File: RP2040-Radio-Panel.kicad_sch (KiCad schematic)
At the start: 1 part, among them U1 DM13A

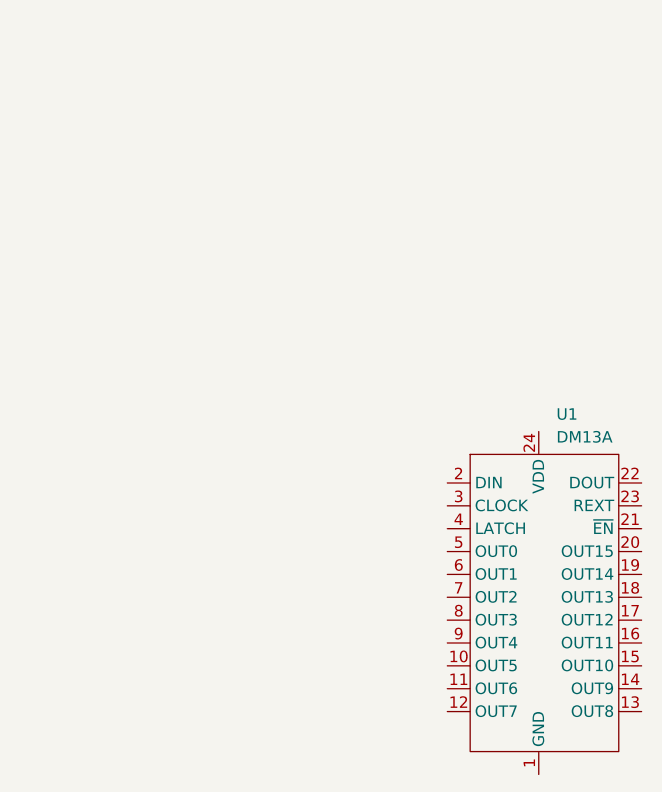
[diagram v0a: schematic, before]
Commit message: Add RP2040
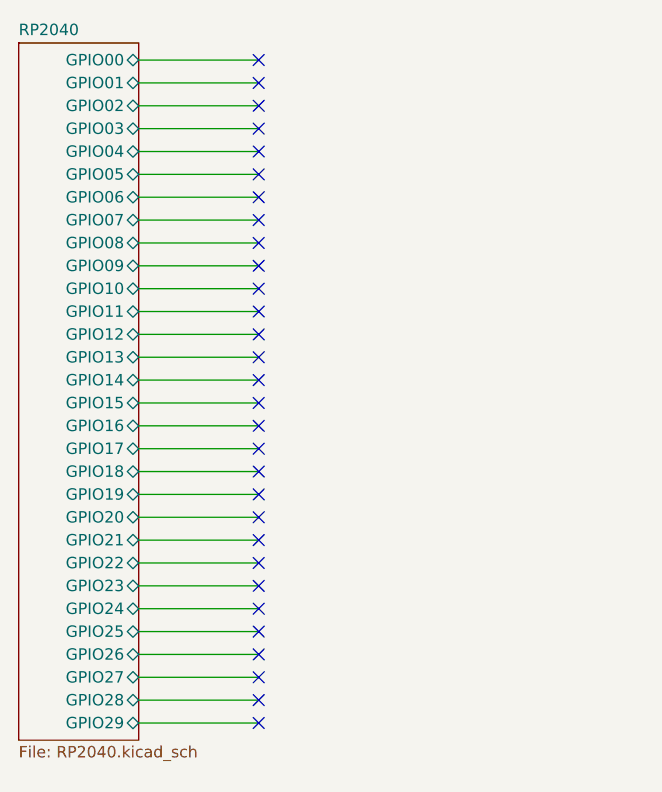
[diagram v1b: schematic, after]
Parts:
- removed U1: DM13A, Package_SO:SSOP-24_3.9x8.7mm_P0.635mm, symbol Custom_Symbols:DM13A
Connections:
- no-connect marks 0 -> 30
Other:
- added sheet RP2040 (RP2040.kicad_sch)

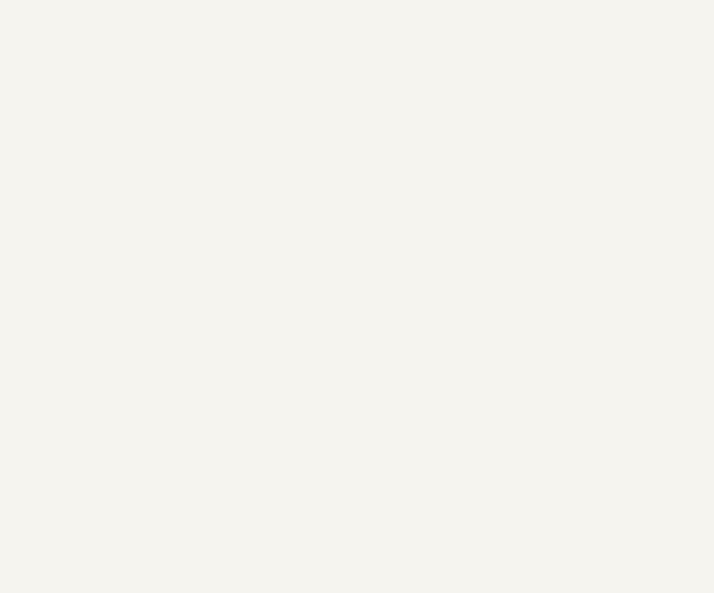
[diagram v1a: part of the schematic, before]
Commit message: Add a level shifter
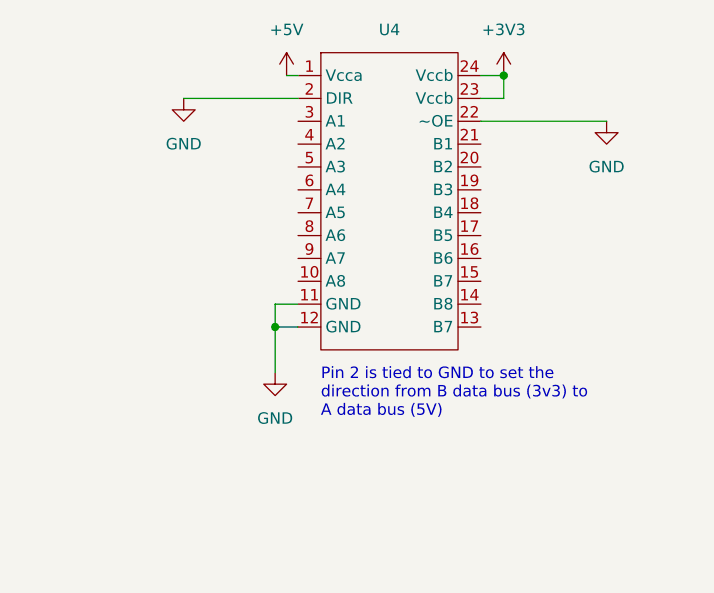
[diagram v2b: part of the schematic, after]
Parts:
- added U4: ~, Package_SO:TSSOP-24_4.4x7.8mm_P0.65mm, symbol Custom_Symbols:SN74LVC4245APWR
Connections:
- new net +3V3: U4.23 (Vccb), U4.24 (Vccb)
- new net +5V: U4.1 (Vcca)
- new net GND: U4.11 (GND), U4.12 (GND), U4.2 (DIR), U4.22 (~OE)
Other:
- note added: "Pin 2 is tied to GND to set the direction from B data bus (3v3) to A data bus (5V)"
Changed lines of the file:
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@@
     (rev "${VERSION}")
+  )
+  (junction (at 113.03 20.32) (diameter 0) (color 0 0 0 0)
+  )
+  (junction (at 87.63 48.26) (diameter 0) (color 0 0 0 0)
   )
   (no_connect (at 41.275 74.93))
@@
     (stroke (width 0) (type default))
   )
+  (wire (pts (xy 110.49 20.32) (xy 113.03 20.32))
+    (stroke (width 0) (type default))
+  )
+  (wire (pts (xy 87.63 48.26) (xy 87.63 53.34))
+    (stroke (width 0) (type default))
+  )
   (wire (pts (xy 27.94 72.39) (xy 41.275 72.39))
     (stroke (width 0) (type default))
   )
+  (wire (pts (xy 77.47 22.86) (xy 90.17 22.86))
+    (stroke (width 0) (type default))
+  )
+  (wire (pts (xy 110.49 22.86) (xy 113.03 22.86))
+    (stroke (width 0) (type default))
+  )
   (wire (pts (xy 27.94 92.71) (xy 41.275 92.71))
     (stroke (width 0) (type default))
@@
     (stroke (width 0) (type default))
   )
+  (wire (pts (xy 88.9 20.32) (xy 90.17 20.32))
+    (stroke (width 0) (type default))
+  )
+  (wire (pts (xy 110.49 25.4) (xy 124.46 25.4))
+    (stroke (width 0) (type default))
+  )
+  (wire (pts (xy 90.17 45.72) (xy 87.63 45.72))
+    (stroke (width 0) (type default))
+  )
   (wire (pts (xy 27.94 69.85) (xy 41.275 69.85))
     (stroke (width 0) (type default))
@@
     (stroke (width 0) (type default))
   )
+  (wire (pts (xy 87.63 48.26) (xy 90.17 48.26))
+    (stroke (width 0) (type default))
+  )
   (wire (pts (xy 27.94 31.75) (xy 41.275 31.75))
     (stroke (width 0) (type default))
   )
+  (wire (pts (xy 87.63 45.72) (xy 87.63 48.26))
+    (stroke (width 0) (type default))
+  )
+  (wire (pts (xy 113.03 22.86) (xy 113.03 20.32))
+    (stroke (width 0) (type default))
+  )
   (wire (pts (xy 27.94 62.23) (xy 41.275 62.23))
     (stroke (width 0) (type default))
@@
     (stroke (width 0) (type default))
   )
+  (text "Pin 2 is tied to GND to set the\ndirection from B data bus (3v3) to\nA data bus (5V)"
+    (at 92.71 58.42 0)
+    (effects (font (size 1.27 1.27)) (justify left bottom))
+  )
+  (symbol (lib_id "power:GND") (at 77.47 22.86 0) (unit 1)
+    (in_bom yes) (on_board yes) (dnp no) (fields_autoplaced)
+    (property "Reference" "#PWR08" (at 77.47 29.21 0)
+      (effects (font (size 1.27 1.27)) hide)
+    )
+    (property "Value" "GND" (at 77.47 27.94 0)
+      (effects (font (size 1.27 1.27)))
+    )
+    (property "Footprint" "" (at 77.47 22.86 0)
+      (effects (font (size 1.27 1.27)) hide)
+    )
+    (property "Datasheet" "" (at 77.47 22.86 0)
+      (effects (font (size 1.27 1.27)) hide)
+    )
+    (pin "1")
+    (instances
+      (project "RP2040-Radio-Panel"
+        (path "/e63e39d7-6ac0-4ffd-8aa3-1841a4541b55"
+          (reference "#PWR08") (unit 1)
+        )
+      )
+    )
+  )
+  (symbol (lib_id "power:+5V") (at 88.9 20.32 0) (unit 1)
+    (in_bom yes) (on_board yes) (dnp no) (fields_autoplaced)
+    (property "Reference" "#PWR03" (at 88.9 24.13 0)
+      (effects (font (size 1.27 1.27)) hide)
+    )
+    (property "Value" "+5V" (at 88.9 15.24 0)
+      (effects (font (size 1.27 1.27)))
+    )
+    (property "Footprint" "" (at 88.9 20.32 0)
+      (effects (font (size 1.27 1.27)) hide)
+    )
+    (property "Datasheet" "" (at 88.9 20.32 0)
+      (effects (font (size 1.27 1.27)) hide)
+    )
+    (pin "1")
+    (instances
+      (project "RP2040-Radio-Panel"
+        (path "/e63e39d7-6ac0-4ffd-8aa3-1841a4541b55"
+          (reference "#PWR03") (unit 1)
+        )
+      )
+    )
+  )
+  (symbol (lib_id "Custom_Symbols:SN74LVC4245APWR") (at 100.33 34.29 0) (unit 1)
+    (in_bom yes) (on_board yes) (dnp no) (fields_autoplaced)
+    (property "Reference" "U4" (at 100.33 15.24 0)
+      (effects (font (size 1.27 1.27)))
+    )
+    (property "Value" "~" (at 90.17 20.32 0)
+      (effects (font (size 1.27 1.27)))
+    )
+    (property "Footprint" "Package_SO:TSSOP-24_4.4x7.8mm_P0.65mm" (at 100.33 55.88 0)
+      (effects (font (size 1.27 1.27)) hide)
+    )
+    (property "Datasheet" "https://www.ti.com/general/docs/suppproductinfo.tsp?distId=10&gotoUrl=https%3A%2F%2Fwww.ti.com%2Flit%2Fgpn%2Fsn74lvc4245a" (at 100.33 53.34 0)
+      (effects (font (size 1.27 1.27)) hide)
+    )
+    (property "MPN - JLCPCB" "C7859" (at 100.33 34.29 0)
+      (effects (font (size 1.27 1.27)) hide)
+    )
+    (pin "1")
+    (pin "10")
+    (pin "11")
+    (pin "12")
+    (pin "13")
+    (pin "14")
+    (pin "15")
+    (pin "16")
+    (pin "17")
+    (pin "18")
+    (pin "19")
+    (pin "2")
+    (pin "20")
+    (pin "21")
+    (pin "22")
+    (pin "23")
+    (pin "24")
+    (pin "3")
+    (pin "4")
+    (pin "5")
+    (pin "6")
+    (pin "7")
+    (pin "8")
+    (pin "9")
+    (instances
+      (project "RP2040-Radio-Panel"
+        (path "/e63e39d7-6ac0-4ffd-8aa3-1841a4541b55"
+          (reference "U4") (unit 1)
+        )
+      )
+    )
+  )
+  (symbol (lib_id "power:+3V3") (at 113.03 20.32 0) (unit 1)
+    (in_bom yes) (on_board yes) (dnp no) (fields_autoplaced)
+    (property "Reference" "#PWR04" (at 113.03 24.13 0)
+      (effects (font (size 1.27 1.27)) hide)
+    )
+    (property "Value" "+3V3" (at 113.03 15.24 0)
+      (effects (font (size 1.27 1.27)))
+    )
+    (property "Footprint" "" (at 113.03 20.32 0)
+      (effects (font (size 1.27 1.27)) hide)
+    )
+    (property "Datasheet" "" (at 113.03 20.32 0)
+      (effects (font (size 1.27 1.27)) hide)
+    )
+    (pin "1")
+    (instances
+      (project "RP2040-Radio-Panel"
+        (path "/e63e39d7-6ac0-4ffd-8aa3-1841a4541b55"
+          (reference "#PWR04") (unit 1)
+        )
+      )
+    )
+  )
+  (symbol (lib_id "power:GND") (at 87.63 53.34 0) (unit 1)
+    (in_bom yes) (on_board yes) (dnp no) (fields_autoplaced)
+    (property "Reference" "#PWR06" (at 87.63 59.69 0)
+      (effects (font (size 1.27 1.27)) hide)
+    )
+    (property "Value" "GND" (at 87.63 58.42 0)
+      (effects (font (size 1.27 1.27)))
+    )
+    (property "Footprint" "" (at 87.63 53.34 0)
+      (effects (font (size 1.27 1.27)) hide)
+    )
+    (property "Datasheet" "" (at 87.63 53.34 0)
+      (effects (font (size 1.27 1.27)) hide)
+    )
+    (pin "1")
+    (instances
+      (project "RP2040-Radio-Panel"
+        (path "/e63e39d7-6ac0-4ffd-8aa3-1841a4541b55"
+          (reference "#PWR06") (unit 1)
+        )
+      )
+    )
+  )
+  (symbol (lib_id "power:GND") (at 124.46 25.4 0) (unit 1)
+    (in_bom yes) (on_board yes) (dnp no) (fields_autoplaced)
+    (property "Reference" "#PWR07" (at 124.46 31.75 0)
+      (effects (font (size 1.27 1.27)) hide)
+    )
+    (property "Value" "GND" (at 124.46 30.48 0)
+      (effects (font (size 1.27 1.27)))
+    )
+    (property "Footprint" "" (at 124.46 25.4 0)
+      (effects (font (size 1.27 1.27)) hide)
+    )
+    (property "Datasheet" "" (at 124.46 25.4 0)
+      (effects (font (size 1.27 1.27)) hide)
+    )
+    (pin "1")
+    (instances
+      (project "RP2040-Radio-Panel"
+        (path "/e63e39d7-6ac0-4ffd-8aa3-1841a4541b55"
+          (reference "#PWR07") (unit 1)
+        )
+      )
+    )
+  )
   (sheet (at 14.605 17.145) (size 13.335 77.47) (fields_autoplaced)

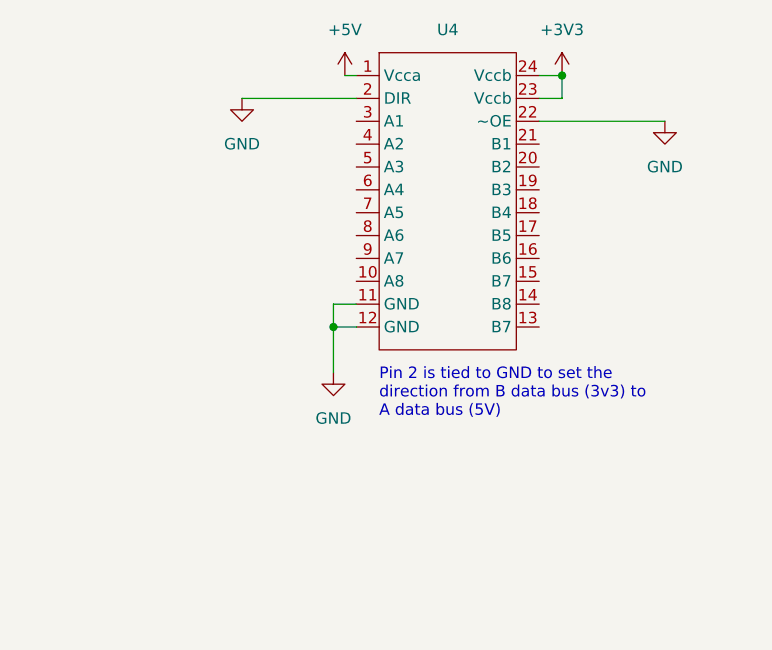
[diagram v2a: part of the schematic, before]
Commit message: Add decoupling capacitors
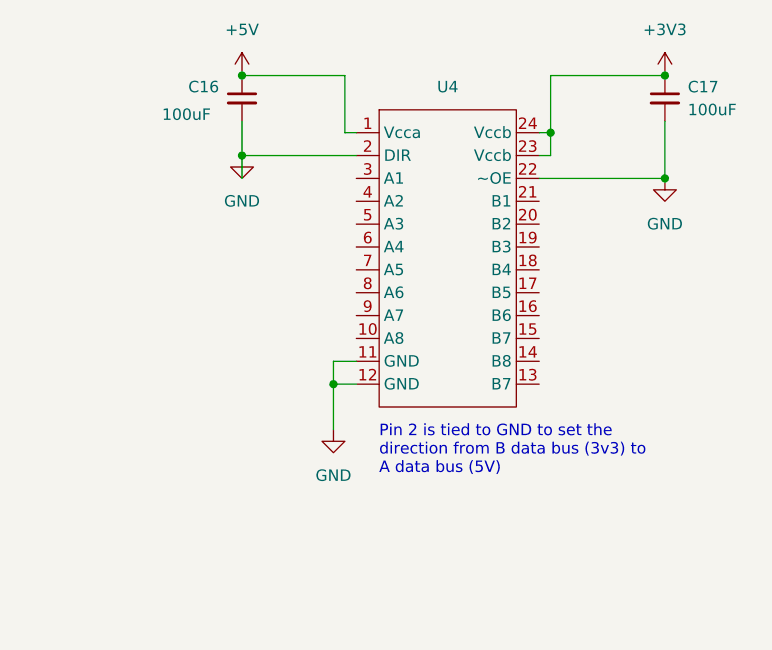
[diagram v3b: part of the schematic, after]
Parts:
- added C16, C17: 100uF, symbol Device:C_Small
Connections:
- net +3V3: now also C17.1
- net +5V: now also C16.1
- net GND: now also C16.2, C17.2
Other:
- moved on the sheet: U4
